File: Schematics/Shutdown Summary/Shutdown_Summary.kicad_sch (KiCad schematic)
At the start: 44 parts, among them J1 GND, J2 TS+, J3 TS-, J4 Main TS Connector, K1 3PoleSwitchingRelay, K2 3PoleSwitchingRelay, K3 Omron DPDT Relay, K4 SPST-NO (Precharge Control), K5 SPST-NO (AIR Control), K6 SPST-NC (Discharge), K7 SPST-NO (Precharge), K8 SPST-NO (AIR), K9 SPST-NO (AIR), SW1 Side BRB, SW10 SMD 1, SW2 Side BRB, SW3 GLVMS, SW4 Brake Over-Travel Switch, SW5 Latching Circuit Reset, SW6 Cockpit BRB, SW7 TSMS, SW8 SMD 2, SW9 HVD, U1 Bender_Isometer_IR155-3204

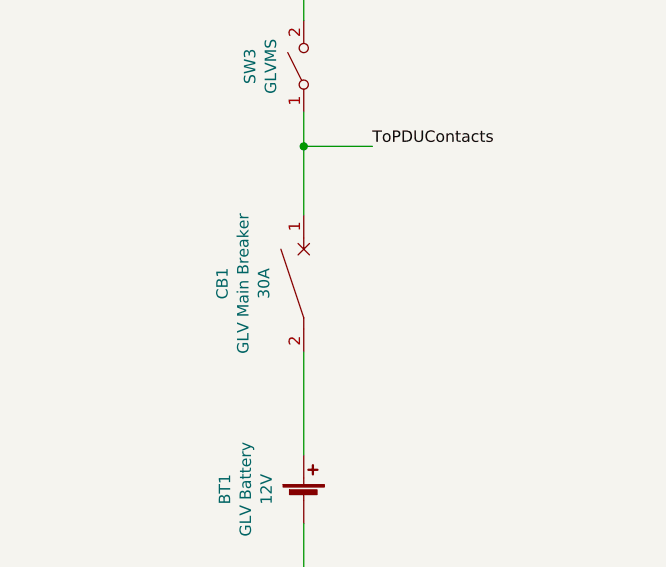
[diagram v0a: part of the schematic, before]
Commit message: Changed breaker to fuse in Shutdown Simmary
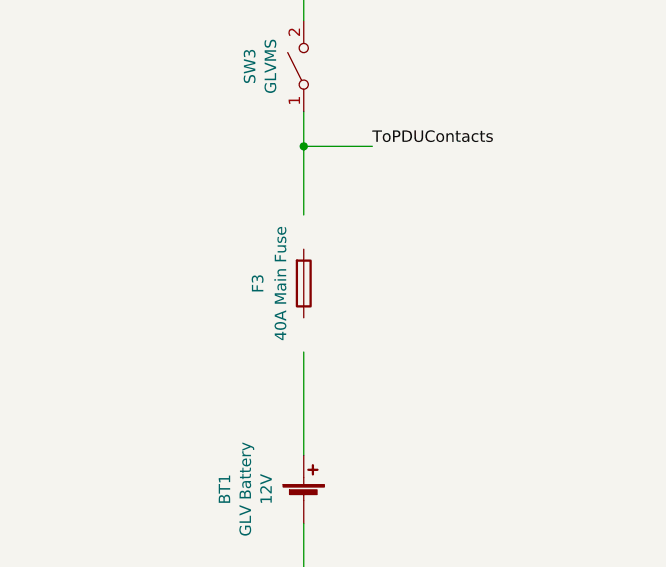
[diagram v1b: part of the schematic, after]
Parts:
- removed CB1: GLV Main Breaker, symbol Device:CircuitBreaker_1P
- added F3: 40A Main Fuse, symbol Device:Fuse
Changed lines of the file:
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@@
   (title_block
     (title "Shutdown Circuit Summary")
-    (date "2023-01-25")
-    (rev "4")
+    (date "2023-02-02")
+    (rev "5")
     (company "Northeastern Electric Racing")
     (comment 1 "https://github.com/Northeastern-Electric-Racing/NER")
@@
     )
     (property "Voltage" "12V" (id 4) (at 44.1198 218.44 90))
-    (pin "1")
-    (pin "2")
-  )
-  (symbol (lib_id "Device:CircuitBreaker_1P") (at 48.26 195.58 0) (unit 1)
-    (in_bom yes) (on_board yes)
-    (property "Reference" "CB1" (id 0) (at 39.2176 195.58 90))
-    (property "Value" "GLV Main Breaker" (id 1) (at 41.529 195.58 90))
-    (property "Footprint" "" (id 2) (at 48.26 195.58 0)
-      (effects (font (size 1.27 1.27)) hide)
-    )
-    (property "Datasheet" "~" (id 3) (at 48.26 195.58 0)
-      (effects (font (size 1.27 1.27)) hide)
-    )
-    (property "Current" "30A" (id 4) (at 43.8404 195.58 90))
     (pin "1")
     (pin "2")
@@
     (pin "2")
   )
+  (symbol (lib_id "Device:Fuse") (at 48.26 195.58 0) (mirror x) (unit 1)
+    (in_bom yes) (on_board yes)
+    (property "Reference" "F3" (id 0) (at 43.18 195.58 90))
+    (property "Value" "40A Main Fuse" (id 1) (at 45.72 195.58 90))
+    (property "Footprint" "" (id 2) (at 46.482 195.58 90)
+      (effects (font (size 1.27 1.27)) hide)
+    )
+    (property "Datasheet" "~" (id 3) (at 48.26 195.58 0)
+      (effects (font (size 1.27 1.27)) hide)
+    )
+    (pin "1")
+    (pin "2")
+  )
   (symbol (lib_id "Relay:G5V-2") (at 214.63 72.39 270) (mirror x) (unit 1)
     (in_bom yes) (on_board yes)
@@
       (reference "BT5") (unit 1) (value "Segement 1 ") (footprint "")
     )
-    (path "/00000000-0000-0000-0000-000076703898"
-      (reference "CB1") (unit 1) (value "GLV Main Breaker") (footprint "")
-    )
     (path "/0435eff0-dc15-4323-bc7d-c33834242e3b"
       (reference "D1") (unit 1) (value "1N4001") (footprint "Diode_THT:D_DO-41_SOD81_P10.16mm_Horizontal")
@@
       (reference "F3") (unit 1) (value "Fuse") (footprint "")
     )
+    (path "/ae8778c1-77f3-4cfe-b88b-36028f00f1b5"
+      (reference "F3") (unit 1) (value "40A Main Fuse") (footprint "")
+    )
     (path "/00000000-0000-0000-0000-0000767039cb"

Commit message: Finished traces
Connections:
- net ToPDUContacts: now also F3.2
- net at BT1.1 (+): now also F3.1
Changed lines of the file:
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@@
     (stroke (width 0.4) (type default) (color 255 153 0 1))
   )
-  (wire (pts (xy 48.26 187.96) (xy 48.26 180.34))
+  (wire (pts (xy 48.26 180.34) (xy 48.26 191.77))
     (stroke (width 0.5) (type default) (color 255 0 255 1))
   )
@@
     (stroke (width 0.4) (type default) (color 255 153 0 1))
   )
-  (wire (pts (xy 48.26 214.63) (xy 48.26 203.2))
+  (wire (pts (xy 48.26 199.39) (xy 48.26 214.63))
     (stroke (width 0.5) (type default) (color 255 0 255 1))
   )

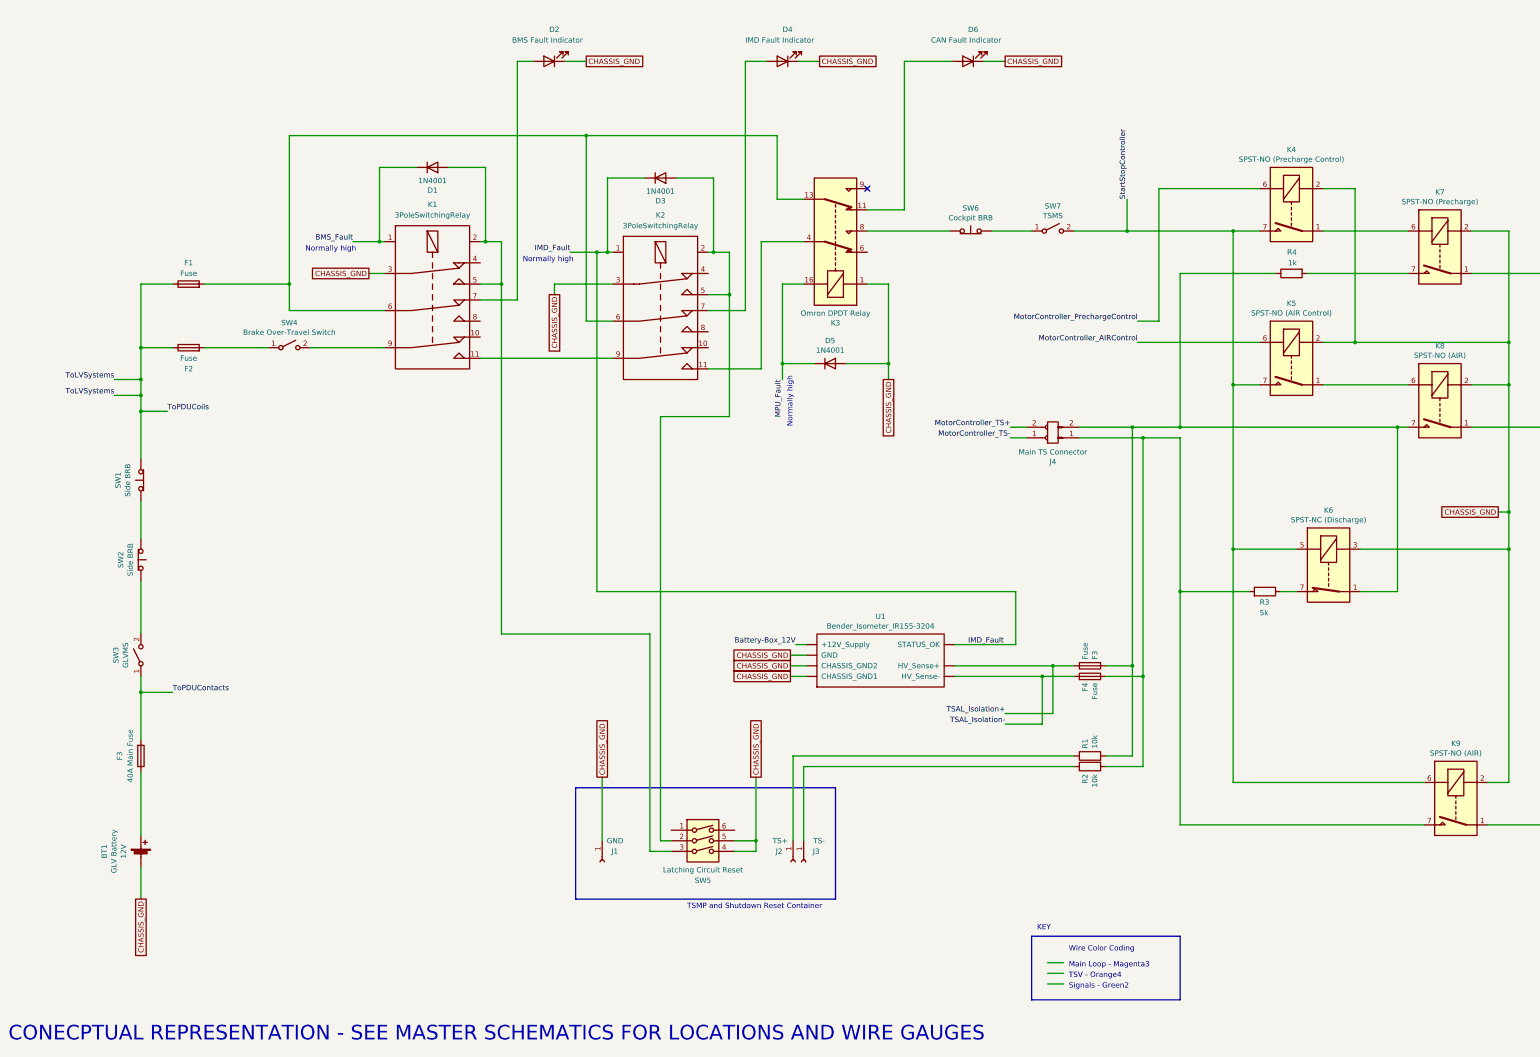
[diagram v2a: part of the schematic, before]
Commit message: Revert "ESF-2 2023 Updates (#136)"
This reverts commit dbac7da28cdaad5f36fde89af32aad76a0b85ea3.
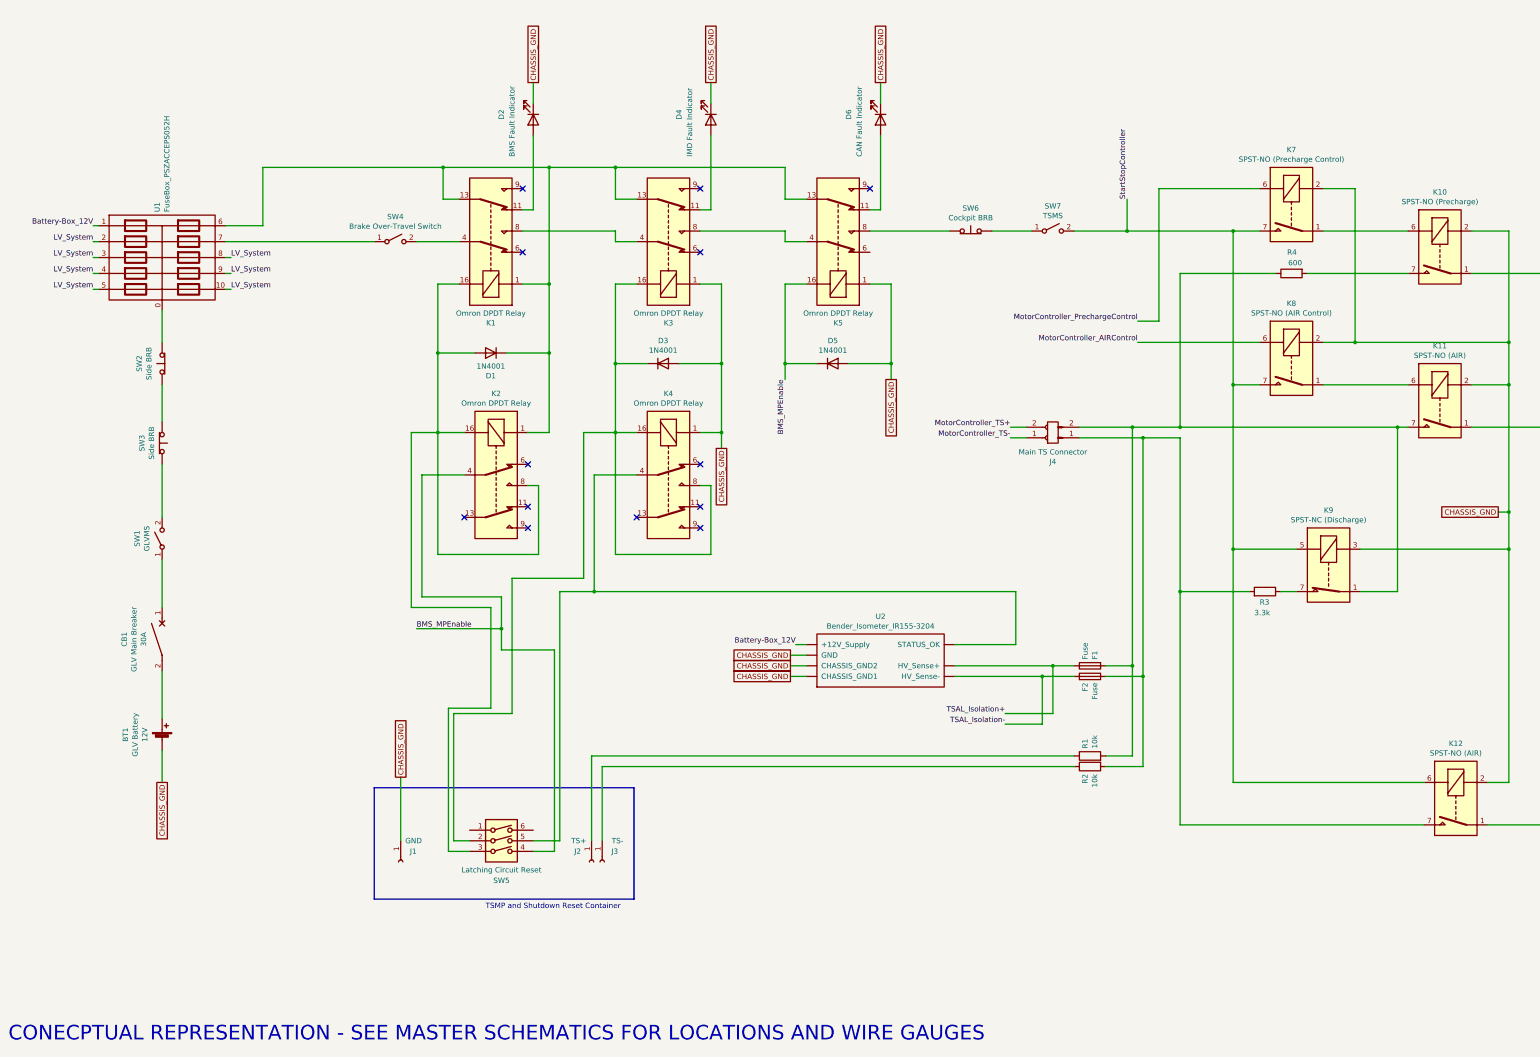
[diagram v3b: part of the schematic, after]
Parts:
- removed F1, F2: Fuse, symbol Device:Fuse
- removed F3: 40A Main Fuse, symbol Device:Fuse
- removed K1, K2: 3PoleSwitchingRelay, symbol NER:3PoleSwitchingRelay
- added CB1: GLV Main Breaker, symbol Device:CircuitBreaker_1P
- added K1, K2, K3, K4: Omron DPDT Relay, Relay_THT:Relay_DPDT_Omron_G5V-2, symbol Relay:G5V-2
- added U1: FuseBox_PSZACCEPS052H, symbol NER:FuseBox_PSZACCEPS052H
- R3: value 5k -> 3.3k
- R4: value 1k -> 600
- renumbered F3 to F1, F4 to F2, K7 to K10, K8 to K11, K9 to K12, K3 to K5, K4 to K7, K5 to K8, K6 to K9, SW3 to SW1, SW1 to SW2, SW2 to SW3, U1 to U2
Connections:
- net BMS_Fault is gone; now on an unnamed net: D1.1 (K)
- net Battery-Box_12V: now also U1.1
- net CHASSIS_GND: now also D3.2 (A), K3.1, K4.1; no longer SW5.4, SW5.5
- net at BT1.1 (+): now also CB1.2
- net at SW4.1 (A): now also U1.7
- net at SW4.2 (B): now also K1.4
- net at D1.2 (A), SW5.3: now also K1.16, K2.16, K2.8
- net at K5.4: now also K3.8
- net at SW5.2: now also D3.1 (K), K3.16, K4.16, K4.8; no longer D3.2 (A)
- net at K5.13: now also K1.1, K1.13, K2.1, K3.13, U1.6
- net at D4.2 (A): now also K3.11
- net at D2.2 (A): now also K1.11
- removed net IMD_Fault: D3.1 (K), U2.~ (STATUS_OK)
- net MPU_Fault renamed BMS_MPEnable
- net BMS_MPEnable: now also SW5.4, K2.4
- net ToLVSystems: no longer names the net of SW2.2 (B)
- net ToLVSystems: now also U1.0
- net ToPDUContacts: no longer names the net of SW1.1 (A)
- net ToPDUContacts: now also CB1.1
- new net: K4.4, SW5.5, U2.~ (STATUS_OK)
- new net: K1.8, K3.4
- new net LV_System: U1.10, U1.2, U1.3, U1.4, U1.5, U1.8, U1.9
- no-connect marks 1 -> 13
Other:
- note removed: "KEY"
- note removed: "Main Loop - Magenta3"
- note removed: "Normally high"
- note removed: "Signals - Green2"
- note removed: "TSV - Orange4"
- note removed: "Wire Color Coding"
- moved on the sheet: BT1, D2, D5, D6, J1, J2, J3, K5, SW1, SW2, SW3, SW4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

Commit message: Shutdown Summary Updates
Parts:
- removed K1, K2, K3, K4: Omron DPDT Relay, Relay_THT:Relay_DPDT_Omron_G5V-2, symbol Relay:G5V-2
- removed U1: FuseBox_PSZACCEPS052H, symbol NER:FuseBox_PSZACCEPS052H
- added F1, F2: Fuse, symbol Device:Fuse
- added K1, K2: 3PoleSwitchingRelay, symbol NER:3PoleSwitchingRelay
- R3: value 3.3k -> 5k
- R4: value 600 -> 1k
- renumbered F1 to F3, F2 to F4, K5 to K3, K7 to K4, K8 to K5, K9 to K6, K10 to K7, K11 to K8, K12 to K9, SW2 to SW1, SW3 to SW2, SW1 to SW3, U2 to U1
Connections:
- net CHASSIS_GND: now also SW5.4, SW5.5, K1.3, K2.3; no longer D3.2 (A)
- net ToPDUContacts: now reaches CB1.1, SW3.1 (A)
- net ToLVSystems: now reaches SW1.2 (B)
- net ToLVSystems: now also F1.1, F2.1
- net at SW4.1 (A): now also F2.2
- net at SW4.2 (B): now also K1.9
- net at K3.13: now also F1.2, K1.6, K2.6; no longer D1.1 (K)
- net at SW5.2: now also D3.2 (A), K2.2, K2.5; no longer D3.1 (K)
- net at D4.2 (A): now also K2.7
- net at K3.4: now also K2.11
- net at D1.2 (A), SW5.3: now also K1.2, K1.5
- net at D2.2 (A): now also K1.7
- net BMS_MPEnable renamed MPU_Fault
- net MPU_Fault: no longer SW5.4
- new net: K1.11, K2.9
- new net BMS_Fault: D1.1 (K), K1.1
- new net IMD_Fault: D3.1 (K), K2.1, U1.~ (STATUS_OK)
- no-connect marks 13 -> 1
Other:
- note added: "KEY"
- note added: "Main Loop - Magenta3"
- note added: "Normally high"
- note added: "Signals - Green2"
- note added: "TSV - Orange4"
- note added: "Wire Color Coding"
- moved on the sheet: BT1, CB1, D2, D5, D6, J1, J2, J3, K3, SW1, SW2, SW3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
